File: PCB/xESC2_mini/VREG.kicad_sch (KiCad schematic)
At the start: 3 parts, among them U2 XC6220B331MR

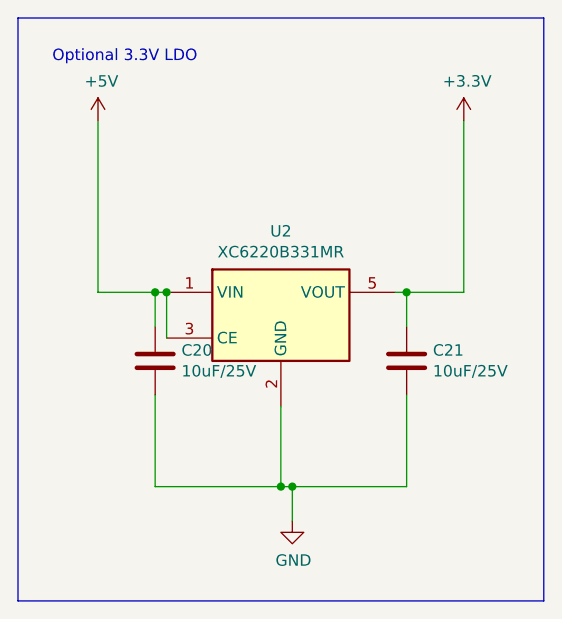
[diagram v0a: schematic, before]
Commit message: wip - most routing for RP2040 done
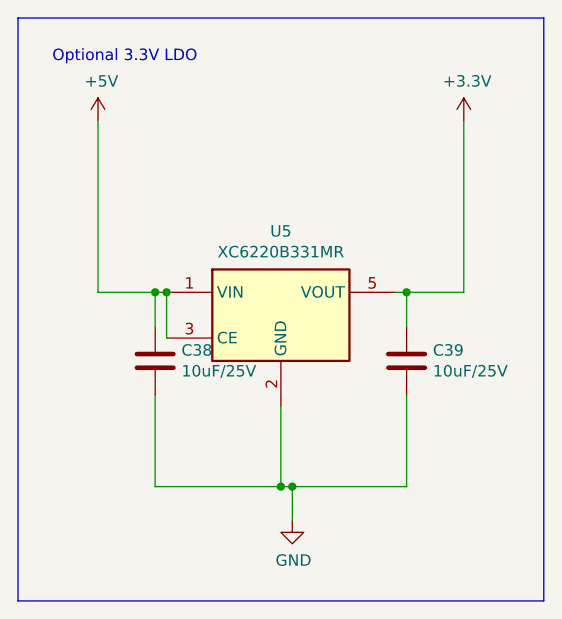
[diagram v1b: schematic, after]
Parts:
- renumbered C20 to C38, C21 to C39, U2 to U5
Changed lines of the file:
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@@
   (symbol (lib_id "power:+3.3V") (at 210.82 71.12 0) (unit 1)
     (in_bom yes) (on_board yes)
-    (property "Reference" "#PWR0111" (id 0) (at 210.82 74.93 0)
+    (property "Reference" "#PWR038" (id 0) (at 210.82 74.93 0)
       (effects (font (size 1.27 1.27)) hide)
     )
@@
   (symbol (lib_id "power:+5V") (at 170.18 71.12 0) (unit 1)
     (in_bom yes) (on_board yes)
-    (property "Reference" "#PWR0112" (id 0) (at 170.18 74.93 0)
+    (property "Reference" "#PWR036" (id 0) (at 170.18 74.93 0)
       (effects (font (size 1.27 1.27)) hide)
     )
@@
   (symbol (lib_id "Device:C") (at 176.53 97.79 0) (unit 1)
     (in_bom yes) (on_board yes)
-    (property "Reference" "C20" (id 0) (at 179.451 96.6216 0)
+    (property "Reference" "C38" (id 0) (at 179.451 96.6216 0)
       (effects (font (size 1.27 1.27)) (justify left))
     )
@@
   (symbol (lib_id "power:GND") (at 191.77 115.57 0) (unit 1)
     (in_bom yes) (on_board yes)
-    (property "Reference" "#PWR0114" (id 0) (at 191.77 121.92 0)
+    (property "Reference" "#PWR037" (id 0) (at 191.77 121.92 0)
       (effects (font (size 1.27 1.27)) hide)
     )
@@
   (symbol (lib_id "Device:C") (at 204.47 97.79 0) (unit 1)
     (in_bom yes) (on_board yes)
-    (property "Reference" "C21" (id 0) (at 207.391 96.6216 0)
+    (property "Reference" "C39" (id 0) (at 207.391 96.6216 0)
       (effects (font (size 1.27 1.27)) (justify left))
     )
@@
   (symbol (lib_id "Regulator_Linear:XC6220B331MR") (at 190.5 92.71 0) (unit 1)
     (in_bom yes) (on_board yes)
-    (property "Reference" "U2" (id 0) (at 190.5 83.3882 0))
+    (property "Reference" "U5" (id 0) (at 190.5 83.3882 0))
     (property "Value" "XC6220B331MR" (id 1) (at 190.5 85.6996 0))
     (property "Footprint" "Package_TO_SOT_SMD:SOT-23-5" (id 2) (at 190.5 92.71 0)
